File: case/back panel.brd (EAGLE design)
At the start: 165 x 30.1 mm, 7 parts, among them J16 8pin

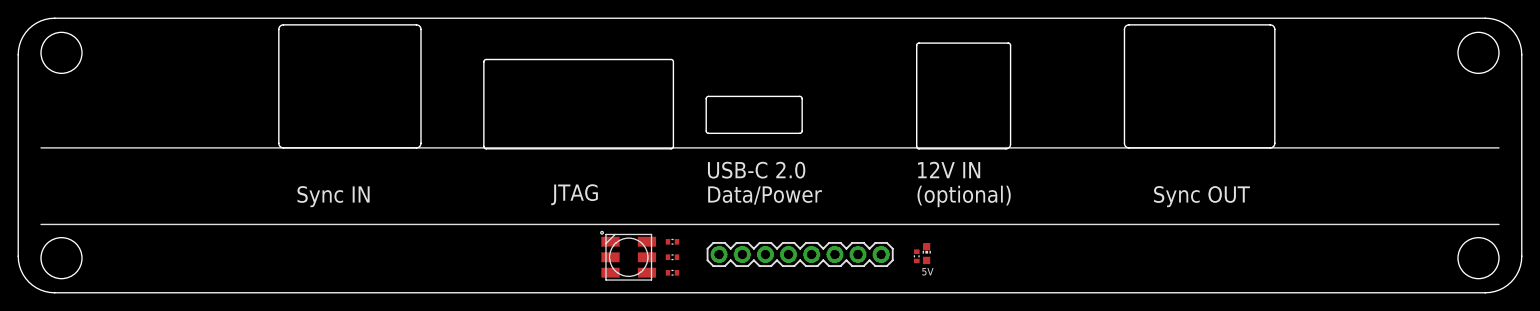
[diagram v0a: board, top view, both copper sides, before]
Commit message: move everything down by 3.5mm (one board slot) to make room for eth connectors
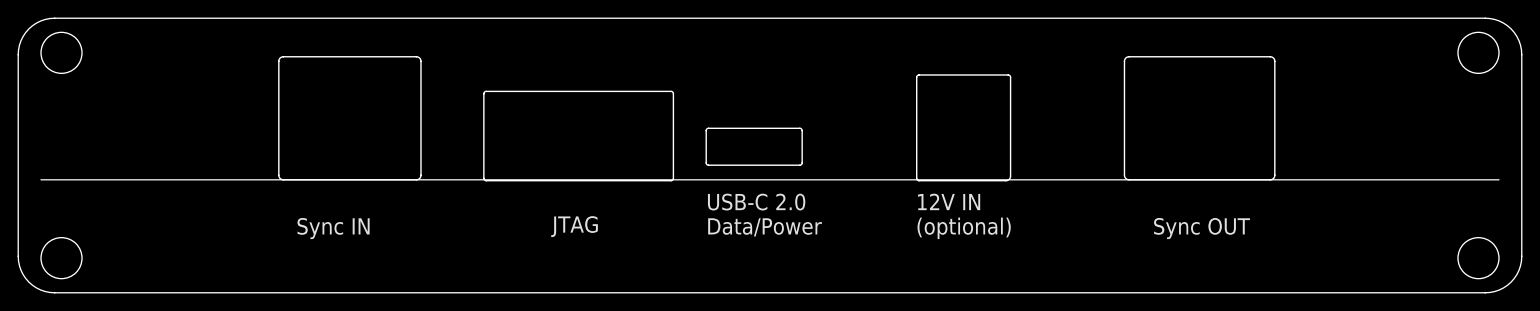
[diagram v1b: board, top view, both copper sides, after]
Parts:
- removed J16: 8pin, SparkFun-Connectors:1X08
- removed LED1: red, adafruit:CHIP-LED0603
- removed LED2: RGBLED5050, adafruit:RGBLED5050
- removed R1, R2, R3, R4: 3.3k, FlashPCB_Resistors:RES-0402
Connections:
- removed net 5V: J16.1, J16.3, J16.5, J16.7, LED1.A
- removed net BLUE: J16.8, R2.P$2
- removed net BLUE_R: LED2.3, R2.P$1
- removed net GND: J16.2, LED2.4, LED2.5, LED2.6, R1.P$1
- removed net GREEN: J16.6, R3.P$2
- removed net GREEN_R: LED2.1, R3.P$1
- removed net N$1: LED1.C, R1.P$2
- removed net RED: J16.4, R4.P$2
- removed net RED_R: LED2.2, R4.P$1
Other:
- outline, holes or cut-outs redrawn
- board text removed: "5V"

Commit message: v1.00
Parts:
- added C2: 10uF, Nordic_nRF:RESC0805_N
- added D1: green, MF_LEDs:LED0805
- added R1: 3.3k, FlashPCB_Resistors:RES-0402
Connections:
- new net 5V: C2.1, D1.ANODE
- new net GND: C2.2, R1.P$1
- new net N$7: D1.CATHODE, R1.P$2
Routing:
- net N$7: track 0.00 -> 11.4 mm
- net 5V: track 0.00 -> 3.52 mm
- net GND: track 0.00 -> 2.34 mm
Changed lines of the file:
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@@
 </autorouter>
 <elements>
+<element name="D1" library="MF_LEDs" package="LED0805" value="green" x="153.3" y="18.4" smashed="yes" rot="MR90">
+<attribute name="HOUSEPART" value="NO" x="159.7" y="15.4" size="1.778" layer="28" rot="MR90" display="off"/>
+<attribute name="MPN" value="" x="159.7" y="15.4" size="1.778" layer="28" rot="MR90" display="off"/>
+<attribute name="POPULATE" value="1" x="159.7" y="15.4" size="1.778" layer="28" rot="MR90" display="off"/>
+<attribute name="URL" value="" x="159.7" y="15.4" size="1.778" layer="28" rot="MR90" display="off"/>
+</element>
+<element name="R1" library="FlashPCB_Resistors" package="RES-0402" value="3.3k" x="144.9" y="19.6" smashed="yes" rot="MR0"/>
+<element name="C2" library="Nordic_nRF" library_urn="urn:adsk.eagle:library:169009" package="RESC0805_N" package3d_urn="urn:adsk.eagle:package:2593736/1" value="10uF" x="148.7" y="19.7" smashed="yes" rot="MR0"/>
 </elements>
 <signals>
 <signal name="SW4">
+</signal>
+<signal name="GND">
+<contactref element="R1" pad="P$1"/>
+<contactref element="C2" pad="2"/>
+<wire x1="147.7" y1="19.7" x2="145.5" y2="19.7" width="0.3048" layer="16"/>
+<wire x1="145.5" y1="19.7" x2="145.4" y2="19.6" width="0.3048" layer="16"/>
+</signal>
+<signal name="5V">
+<contactref element="D1" pad="ANODE"/>
+<contactref element="C2" pad="1"/>
+<wire x1="153.3" y1="19.65" x2="149.85" y2="19.65" width="0.3048" layer="16"/>
+<wire x1="149.85" y1="19.65" x2="149.8" y2="19.7" width="0.3048" layer="16"/>
+</signal>
+<signal name="N$7">
+<contactref element="D1" pad="CATHODE"/>
+<contactref element="R1" pad="P$2"/>
+<wire x1="144.4" y1="19.6" x2="144.4" y2="17.2" width="0.3048" layer="16"/>
+<wire x1="144.4" y1="17.2" x2="144.5" y2="17.1" width="0.3048" layer="16"/>
+<wire x1="144.5" y1="17.1" x2="153.25" y2="17.1" width="0.3048" layer="16"/>
+<wire x1="153.25" y1="17.1" x2="153.3" y2="17.15" width="0.3048" layer="16"/>
 </signal>
 </signals>
@@
 which will not be processed correctly with this version.
 </note>
+<note version="8.2" severity="warning">
+Since Version 8.2, EAGLE supports online libraries. The ids
+of those online libraries will not be understood (or retained)
+with this version.
+</note>
 <note version="8.3" severity="warning">
 Since Version 8.3, EAGLE supports Fusion synchronisation.
@@
 the document will break the link to the Fusion PCB feature.
 </note>
+<note version="8.3" severity="warning">
+Since Version 8.3, EAGLE supports URNs for individual library
+assets (packages, symbols, and devices). The URNs of those assets
+will not be understood (or retained) with this version.
+</note>
+<note version="8.3" severity="warning">
+Since Version 8.3, EAGLE supports the association of 3D packages
+with devices in libraries, schematics, and board files. Those 3D
+packages will not be understood (or retained) with this version.
+</note>
 </compatibility>
